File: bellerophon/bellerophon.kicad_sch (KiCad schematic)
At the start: 16 parts

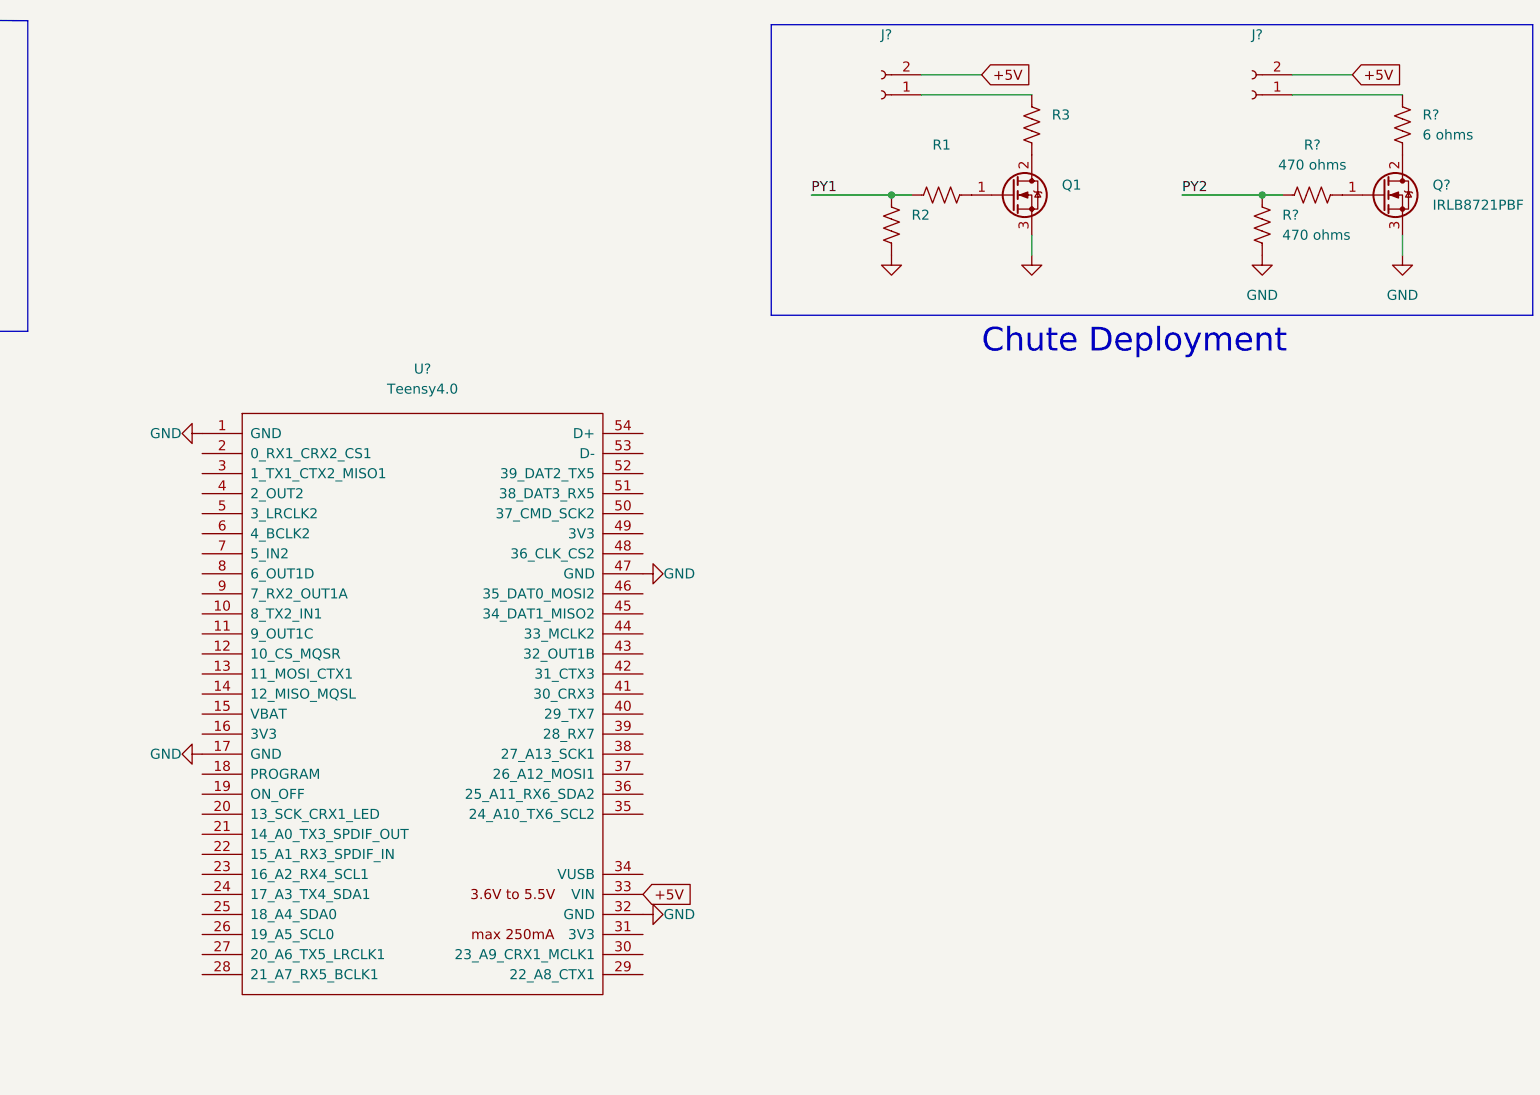
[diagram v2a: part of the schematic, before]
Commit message: connected PY1 and PY2 pins to teensy
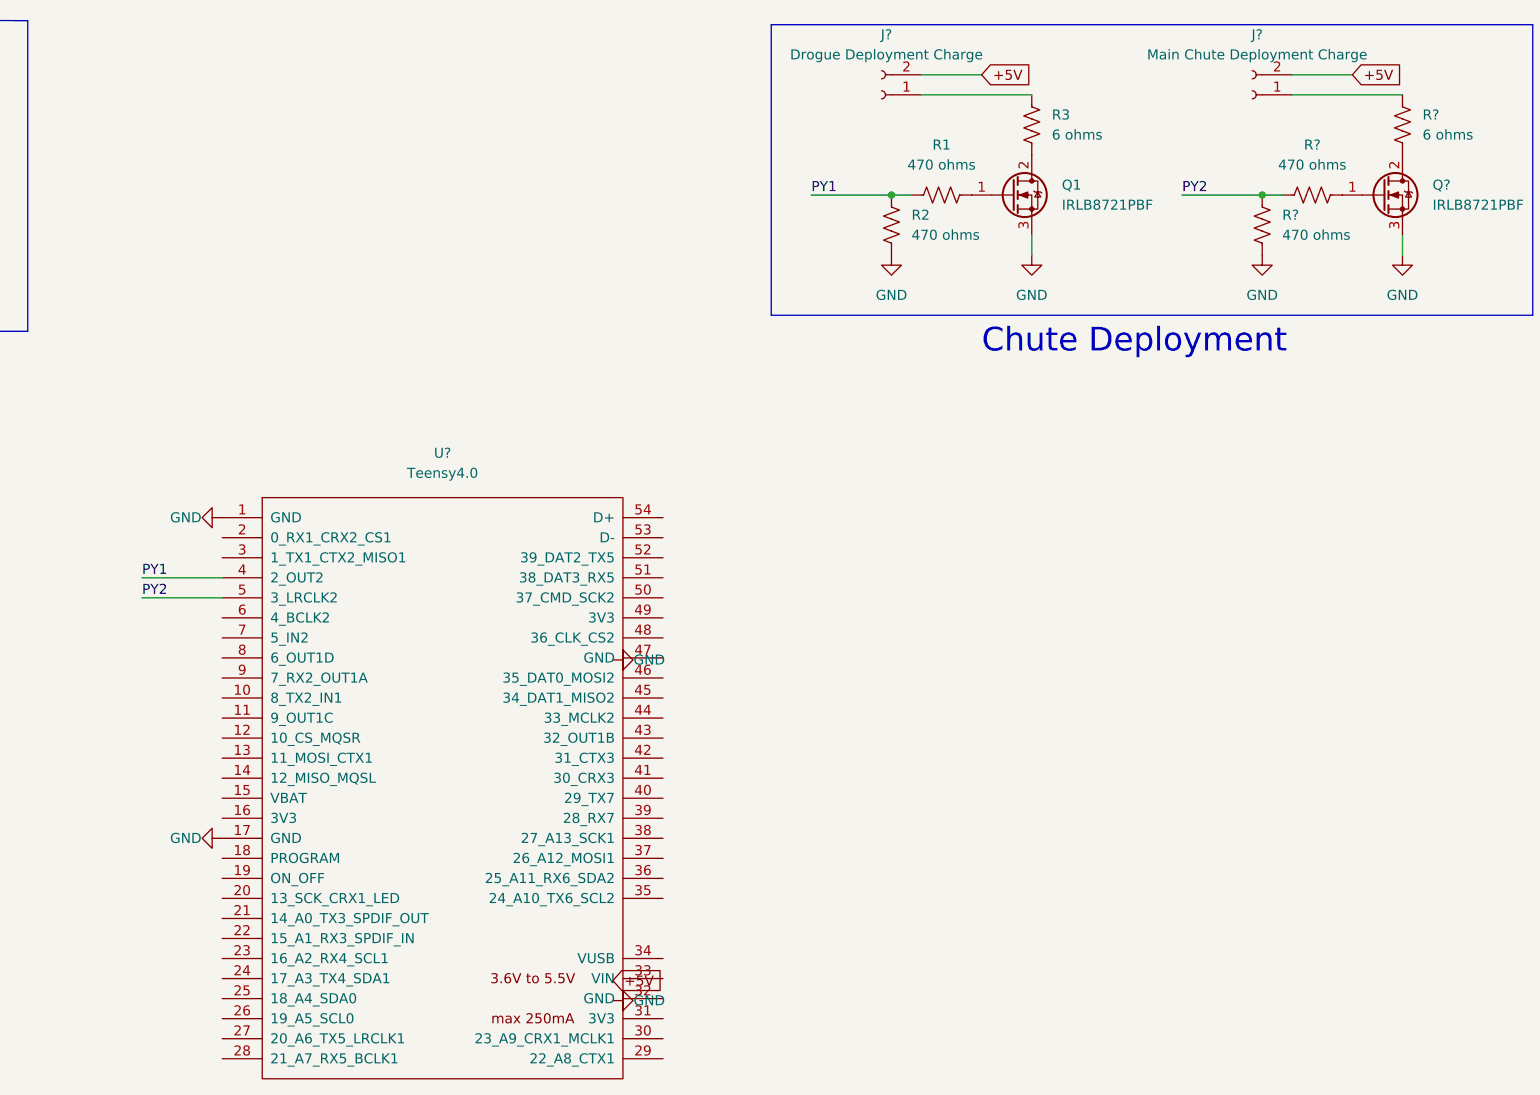
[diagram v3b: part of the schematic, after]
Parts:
- J?: value (none) -> Main Chute Deployment Charge
- J?: value (none) -> Drogue Deployment Charge
- Q1: value (none) -> IRLB8721PBF; footprint (none) -> Package_TO_SOT_THT:TO-220-3_Vertical
- R1, R2: value (none) -> 470 ohms
- R3: value (none) -> 6 ohms
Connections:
- net +5V: no longer U?.33 (VIN)
- net GND: no longer U?.32 (GND), U?.47 (GND)
- net PY1: now also U?.4 (2_OUT2)
- net PY2: now also U?.5 (3_LRCLK2)
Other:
- moved on the sheet: U?
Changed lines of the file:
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@@
+    (stroke (width 0) (type default) (color 0 0 0 0))
+  )
+  (wire (pts (xy 108.204 86.614) (xy 118.364 86.614))
     (stroke (width 0) (type default) (color 0 0 0 0))
   )
@@
   )
   (polyline (pts (xy 93.726 52.832) (xy 12.7 52.832))
+    (stroke (width 0) (type default) (color 0 0 0 0))
+  )
+  (wire (pts (xy 108.204 84.074) (xy 118.364 84.074))
     (stroke (width 0) (type default) (color 0 0 0 0))
   )
@@
   )
   (label "PY1" (at 355.6 15.24 0)
+    (effects (font (size 1.27 1.27)) (justify left bottom))
+  )
+  (label "PY1" (at 108.204 84.074 0)
+    (effects (font (size 1.27 1.27)) (justify left bottom))
+  )
+  (label "PY2" (at 108.204 86.614 0)
     (effects (font (size 1.27 1.27)) (justify left bottom))
   )
@@
     )
   )
-  (global_label "+5V" (shape input) (at 171.704 124.206 0) (fields_autoplaced)
+  (global_label "+5V" (shape input) (at 167.894 135.128 0) (fields_autoplaced)
     (effects (font (size 1.27 1.27)) (justify left))
-    (property "Intersheet References" "${INTERSHEET_REFS}" (id 0) (at 177.9876 124.2854 0)
+    (property "Intersheet References" "${INTERSHEET_REFS}" (id 0) (at 174.1776 135.2074 0)
       (effects (font (size 1.27 1.27)) (justify left) hide)
     )
@@
     (pin "1")
   )
-  (symbol (lib_id "power:GND") (at 115.824 65.786 270) (unit 1)
-    (in_bom yes) (on_board yes)
-    (property "Reference" "#PWR?" (id 0) (at 109.474 65.786 0)
-      (effects (font (size 1.27 1.27)) hide)
-    )
-    (property "Value" "GND" (id 1) (at 109.22 65.786 90)
-      (effects (font (size 1.27 1.27)) (justify left))
-    )
-    (property "Footprint" "" (id 2) (at 115.824 65.786 0)
-      (effects (font (size 1.27 1.27)) hide)
-    )
-    (property "Datasheet" "" (id 3) (at 115.824 65.786 0)
+  (symbol (lib_id "power:GND") (at 118.364 76.454 270) (unit 1)
+    (in_bom yes) (on_board yes)
+    (property "Reference" "#PWR?" (id 0) (at 112.014 76.454 0)
+      (effects (font (size 1.27 1.27)) hide)
+    )
+    (property "Value" "GND" (id 1) (at 111.76 76.454 90)
+      (effects (font (size 1.27 1.27)) (justify left))
+    )
+    (property "Footprint" "" (id 2) (at 118.364 76.454 0)
+      (effects (font (size 1.27 1.27)) hide)
+    )
+    (property "Datasheet" "" (id 3) (at 118.364 76.454 0)
       (effects (font (size 1.27 1.27)) hide)
     )
@@
     (pin "3")
   )
-  (symbol (lib_id "power:GND") (at 171.704 83.566 90) (unit 1)
-    (in_bom yes) (on_board yes)
-    (property "Reference" "#PWR?" (id 0) (at 178.054 83.566 0)
-      (effects (font (size 1.27 1.27)) hide)
-    )
-    (property "Value" "GND" (id 1) (at 178.308 83.566 90)
-      (effects (font (size 1.27 1.27)) (justify left))
-    )
-    (property "Footprint" "" (id 2) (at 171.704 83.566 0)
-      (effects (font (size 1.27 1.27)) hide)
-    )
-    (property "Datasheet" "" (id 3) (at 171.704 83.566 0)
+  (symbol (lib_id "power:GND") (at 167.894 94.488 90) (unit 1)
+    (in_bom yes) (on_board yes)
+    (property "Reference" "#PWR?" (id 0) (at 174.244 94.488 0)
+      (effects (font (size 1.27 1.27)) hide)
+    )
+    (property "Value" "GND" (id 1) (at 174.498 94.488 90)
+      (effects (font (size 1.27 1.27)) (justify left))
+    )
+    (property "Footprint" "" (id 2) (at 167.894 94.488 0)
+      (effects (font (size 1.27 1.27)) hide)
+    )
+    (property "Datasheet" "" (id 3) (at 167.894 94.488 0)
       (effects (font (size 1.27 1.27)) hide)
     )
@@
       (effects (font (size 1.27 1.27)) (justify left))
     )
-    (property "Value" "" (id 1) (at 224.79 36.8299 0)
-      (effects (font (size 1.27 1.27)) (justify left))
-    )
-    (property "Footprint" "" (id 2) (at 224.79 37.465 0)
+    (property "Value" "IRLB8721PBF" (id 1) (at 224.79 36.8299 0)
+      (effects (font (size 1.27 1.27)) (justify left))
+    )
+    (property "Footprint" "Package_TO_SOT_THT:TO-220-3_Vertical" (id 2) (at 224.79 37.465 0)
       (effects (font (size 1.27 1.27) italic) (justify left) hide)
     )
@@
     (in_bom yes) (on_board yes) (fields_autoplaced)
     (property "Reference" "R1" (id 0) (at 209.55 29.21 90))
-    (property "Value" "" (id 1) (at 209.55 31.75 90))
+    (property "Value" "470 ohms" (id 1) (at 209.55 31.75 90))
     (property "Footprint" "" (id 2) (at 209.804 34.544 90)
       (effects (font (size 1.27 1.27)) hide)
@@
     (in_bom yes) (on_board yes) (fields_autoplaced)
     (property "Reference" "J?" (id 0) (at 249.555 15.24 0))
-    (property "Value" "" (id 1) (at 249.555 17.78 0))
+    (property "Value" "Main Chute Deployment Charge" (id 1) (at 249.555 17.78 0))
     (property "Footprint" "" (id 2) (at 248.92 22.86 0)
       (effects (font (size 1.27 1.27)) hide)
@@
       (effects (font (size 1.27 1.27)) hide)
     )
-    (property "Value" "" (id 1) (at 220.98 48.26 0))
+    (property "Value" "GND" (id 1) (at 220.98 48.26 0))
     (property "Footprint" "" (id 2) (at 220.98 43.18 0)
       (effects (font (size 1.27 1.27)) hide)
@@
       (effects (font (size 1.27 1.27)) (justify right))
     )
-    (property "Value" "" (id 1) (at 205.74 40.6399 0)
+    (property "Value" "470 ohms" (id 1) (at 205.74 40.6399 0)
       (effects (font (size 1.27 1.27)) (justify right))
     )
@@
       (effects (font (size 1.27 1.27)) hide)
     )
-    (property "Value" "" (id 1) (at 203.2 48.26 0))
+    (property "Value" "GND" (id 1) (at 203.2 48.26 0))
     (property "Footprint" "" (id 2) (at 203.2 43.18 0)
       (effects (font (size 1.27 1.27)) hide)
@@
     (pin "1")
   )
-  (symbol (lib_id "power:GND") (at 115.824 106.426 270) (unit 1)
-    (in_bom yes) (on_board yes)
-    (property "Reference" "#PWR?" (id 0) (at 109.474 106.426 0)
-      (effects (font (size 1.27 1.27)) hide)
-    )
-    (property "Value" "GND" (id 1) (at 109.22 106.426 90)
-      (effects (font (size 1.27 1.27)) (justify left))
-    )
-    (property "Footprint" "" (id 2) (at 115.824 106.426 0)
-      (effects (font (size 1.27 1.27)) hide)
-    )
-    (property "Datasheet" "" (id 3) (at 115.824 106.426 0)
+  (symbol (lib_id "power:GND") (at 118.364 117.094 270) (unit 1)
+    (in_bom yes) (on_board yes)
+    (property "Reference" "#PWR?" (id 0) (at 112.014 117.094 0)
+      (effects (font (size 1.27 1.27)) hide)
+    )
+    (property "Value" "GND" (id 1) (at 111.76 117.094 90)
+      (effects (font (size 1.27 1.27)) (justify left))
+    )
+    (property "Footprint" "" (id 2) (at 118.364 117.094 0)
+      (effects (font (size 1.27 1.27)) hide)
+    )
+    (property "Datasheet" "" (id 3) (at 118.364 117.094 0)
       (effects (font (size 1.27 1.27)) hide)
     )
@@
       (effects (font (size 1.27 1.27)) (justify right))
     )
-    (property "Value" "" (id 1) (at 223.52 27.9399 0)
+    (property "Value" "6 ohms" (id 1) (at 223.52 27.9399 0)
       (effects (font (size 1.27 1.27)) (justify right))
     )
@@
     (pin "2")
   )
-  (symbol (lib_id "power:GND") (at 171.704 126.746 90) (unit 1)
-    (in_bom yes) (on_board yes)
-    (property "Reference" "#PWR?" (id 0) (at 178.054 126.746 0)
-      (effects (font (size 1.27 1.27)) hide)
-    )
-    (property "Value" "GND" (id 1) (at 178.308 126.746 90)
-      (effects (font (size 1.27 1.27)) (justify left))
-    )
-    (property "Footprint" "" (id 2) (at 171.704 126.746 0)
-      (effects (font (size 1.27 1.27)) hide)
-    )
-    (property "Datasheet" "" (id 3) (at 171.704 126.746 0)
+  (symbol (lib_id "power:GND") (at 167.894 137.668 90) (unit 1)
+    (in_bom yes) (on_board yes)
+    (property "Reference" "#PWR?" (id 0) (at 174.244 137.668 0)
+      (effects (font (size 1.27 1.27)) hide)
+    )
+    (property "Value" "GND" (id 1) (at 174.498 137.668 90)
+      (effects (font (size 1.27 1.27)) (justify left))
+    )
+    (property "Footprint" "" (id 2) (at 167.894 137.668 0)
+      (effects (font (size 1.27 1.27)) hide)
+    )
+    (property "Datasheet" "" (id 3) (at 167.894 137.668 0)
       (effects (font (size 1.27 1.27)) hide)
     )
@@
     (pin "2")
   )
-  (symbol (lib_id "teensy:Teensy4.0") (at 143.764 100.076 0) (unit 1)
-    (in_bom yes) (on_board yes) (fields_autoplaced)
-    (property "Reference" "U?" (id 0) (at 143.764 57.6072 0))
-    (property "Value" "Teensy4.0" (id 1) (at 143.764 60.1472 0))
-    (property "Footprint" "" (id 2) (at 133.604 94.996 0)
-      (effects (font (size 1.27 1.27)) hide)
-    )
-    (property "Datasheet" "" (id 3) (at 133.604 94.996 0)
+  (symbol (lib_id "teensy:Teensy4.0") (at 146.304 110.744 0) (unit 1)
+    (in_bom yes) (on_board yes) (fields_autoplaced)
+    (property "Reference" "U?" (id 0) (at 146.304 68.2752 0))
+    (property "Value" "Teensy4.0" (id 1) (at 146.304 70.8152 0))
+    (property "Footprint" "" (id 2) (at 136.144 105.664 0)
+      (effects (font (size 1.27 1.27)) hide)
+    )
+    (property "Datasheet" "" (id 3) (at 136.144 105.664 0)
       (effects (font (size 1.27 1.27)) hide)
     )
@@
     (in_bom yes) (on_board yes) (fields_autoplaced)
     (property "Reference" "J?" (id 0) (at 202.565 15.24 0))
-    (property "Value" "" (id 1) (at 202.565 17.78 0))
+    (property "Value" "Drogue Deployment Charge" (id 1) (at 202.565 17.78 0))
     (property "Footprint" "" (id 2) (at 201.93 22.86 0)
       (effects (font (size 1.27 1.27)) hide)
